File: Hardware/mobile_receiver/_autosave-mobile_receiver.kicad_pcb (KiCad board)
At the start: 4 copper layers, 82.5 x 142 mm, 33 parts, among them J1 Conn_02x07_Top_Bottom, SW1 SW_SPST, SW2 SW_Push, SW3 SW_Push, SW4 SW_Push, SW5 SW_Push, SW6 SW_Push, SW7 SW_Push, U2 kb2040

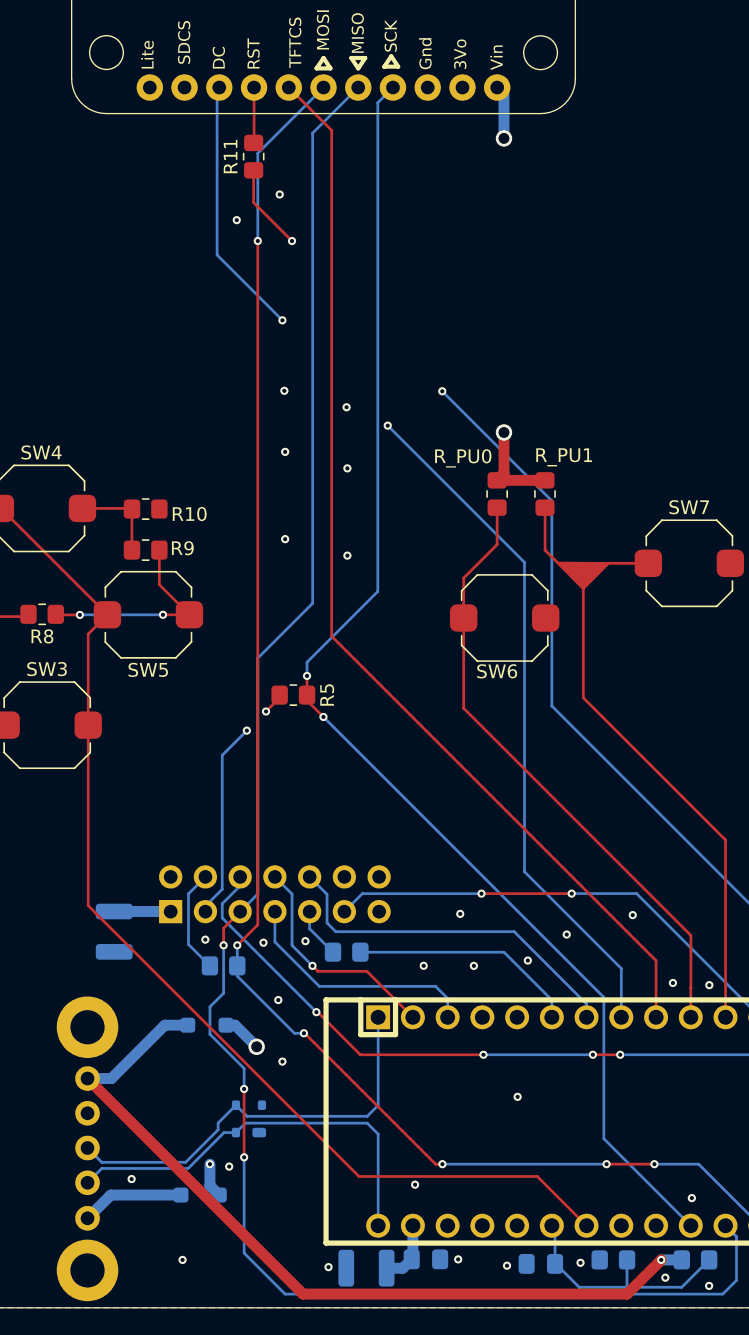
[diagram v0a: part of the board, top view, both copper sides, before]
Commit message: Refined Stitching Vias
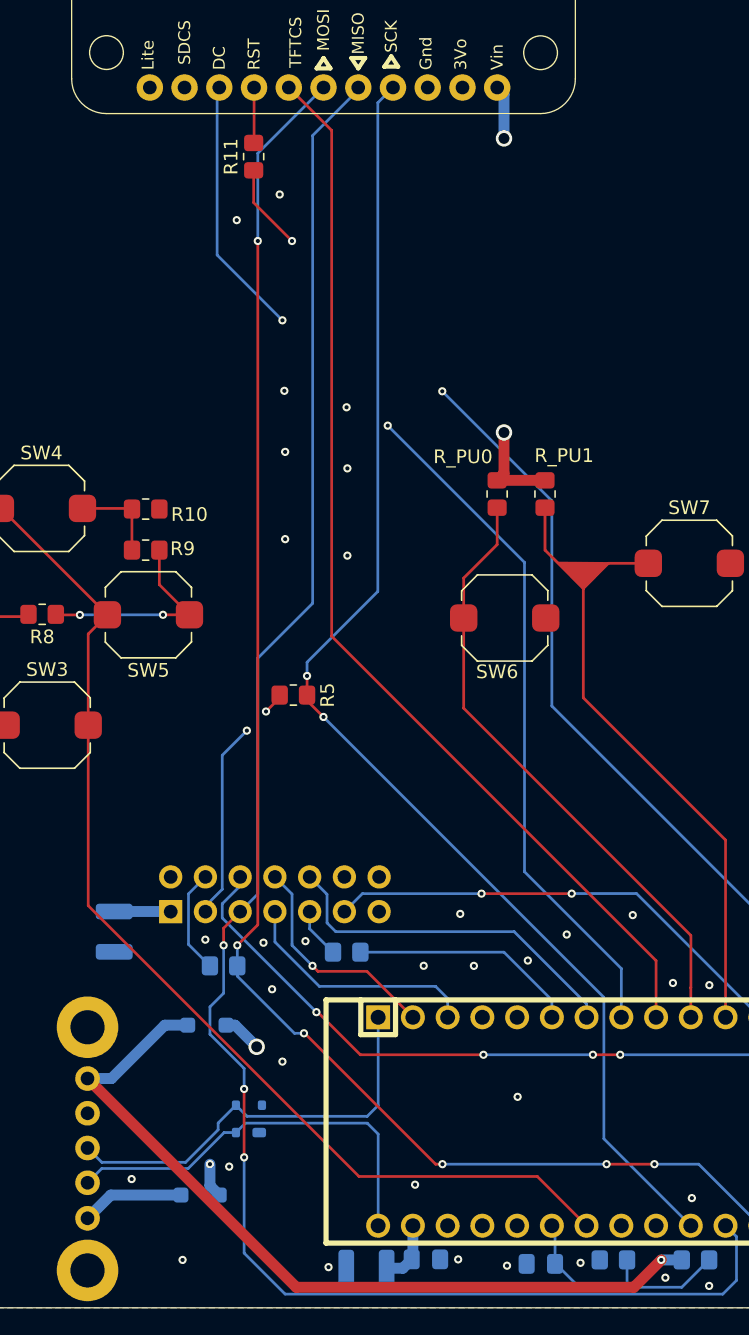
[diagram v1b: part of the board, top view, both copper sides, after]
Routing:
- net +3.3V: track 147.4 -> 148.1 mm
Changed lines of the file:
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@@
 			)
 		)
-		(fp_text user "RT"
-			(at -16.985573 15.83562 90)
-			(unlocked yes)
-			(layer "B.SilkS")
-			(effects
-				(font
-					(size 0.87376 0.87376)
-					(thickness 0.14224)
-				)
-				(justify left mirror)
-			)
-		)
-		(fp_text user "CK"
-			(at -6.825573 15.83562 90)
-			(unlocked yes)
-			(layer "B.SilkS")
-			(effects
-				(font
-					(size 0.87376 0.87376)
-					(thickness 0.14224)
-				)
-				(justify left mirror)
-			)
-		)
-		(fp_text user "SI"
-			(at -11.905573 15.83562 90)
-			(unlocked yes)
-			(layer "B.SilkS")
-			(effects
-				(font
-					(size 0.87376 0.87376)
-					(thickness 0.14224)
-				)
-				(justify left mirror)
-			)
-		)
-		(fp_text user "CC"
-			(at -22.065573 15.83562 90)
-			(unlocked yes)
-			(layer "B.SilkS")
-			(effects
-				(font
-					(size 0.87376 0.87376)
-					(thickness 0.14224)
-				)
-				(justify left mirror)
-			)
-		)
-		(fp_text user "SO"
-			(at -9.365573 15.83562 90)
-			(unlocked yes)
-			(layer "B.SilkS")
-			(effects
-				(font
-					(size 0.87376 0.87376)
-					(thickness 0.14224)
-				)
-				(justify left mirror)
-			)
-		)
-		(fp_text user "V+"
-			(at 0.794427 15.83562 90)
-			(unlocked yes)
-			(layer "B.SilkS")
-			(effects
-				(font
-					(size 0.87376 0.87376)
-					(thickness 0.14224)
-				)
-				(justify left mirror)
-			)
-		)
-		(fp_text user "BL"
-			(at -24.605573 15.83562 90)
-			(unlocked yes)
-			(layer "B.SilkS")
-			(effects
-				(font
-					(size 0.87376 0.87376)
-					(thickness 0.14224)
-				)
-				(justify left mirror)
-			)
-		)
-		(fp_text user "3V"
-			(at -1.745573 15.83562 90)
-			(unlocked yes)
-			(layer "B.SilkS")
-			(effects
-				(font
-					(size 0.87376 0.87376)
-					(thickness 0.14224)
-				)
-				(justify left mirror)
-			)
-		)
-		(fp_text user "G"
-			(at -4.285573 15.83562 90)
-			(unlocked yes)
-			(layer "B.SilkS")
-			(effects
-				(font
-					(size 0.87376 0.87376)
-					(thickness 0.14224)
-				)
-				(justify left mirror)
-			)
-		)
-		(fp_text user "TC"
-			(at -14.445573 15.83562 90)
-			(unlocked yes)
-			(layer "B.SilkS")
-			(effects
-				(font
-					(size 0.87376 0.87376)
-					(thickness 0.14224)
-				)
-				(justify left mirror)
-			)
-		)
-		(fp_text user "DC"
-			(at -19.525573 15.83562 90)
-			(unlocked yes)
-			(layer "B.SilkS")
-			(effects
-				(font
-					(size 0.87376 0.87376)
-					(thickness 0.14224)
-				)
-				(justify left mirror)
-			)
-		)
 		(pad "1" thru_hole circle
 			(at 0.794427 16.97862 270)
@@
 	)
 	(via
-		(at 204.5 199.5)
+		(at 204.045384 198.709131)
 		(size 0.6)
 		(drill 0.3)
@@
 	)
 	(segment
-		(start 230 221)
-		(end 206.311557 221)
+		(start 205.811557 220.5)
+		(end 190.549921 205.238364)
 		(width 0.8)
 		(layer "F.Cu")
@@
 	)
 	(segment
-		(start 206.311557 221)
-		(end 190.549921 205.238364)
+		(start 230.5 220.5)
+		(end 205.811557 220.5)
 		(width 0.8)
 		(layer "F.Cu")
@@
 	(segment
 		(start 232.5 218.5)
-		(end 230 221)
+		(end 230.5 220.5)
 		(width 0.8)
 		(layer "F.Cu")
@@
 	)
 	(segment
-		(start 203 191.747824)
-		(end 203 174.5)
-		(width 0.2)
-		(layer "B.Cu")
-		(net 14)
-	)
-	(segment
 		(start 237 221)
 		(end 205 221)
@@
 	)
 	(segment
-		(start 207.01 170.49)
-		(end 207.01 136.113047)
+		(start 207.01 136.287009)
+		(end 210.344427 132.952582)
 		(width 0.2)
 		(layer "B.Cu")
@@
 	)
 	(segment
+		(start 207.01 170.49)
+		(end 207.01 136.287009)
+		(width 0.2)
+		(layer "B.Cu")
+		(net 14)
+	)
+	(segment
 		(start 199.5 202)
 		(end 199.5 200)
@@
 	)
 	(segment
-		(start 207.01 136.113047)
-		(end 210.344427 132.77862)
+		(start 202 218)
+		(end 202 211)
 		(width 0.2)
 		(layer "B.Cu")
@@
 	)
 	(segment
-		(start 201.710805 193.037019)
-		(end 203 191.747824)
+		(start 238 220)
+		(end 237 221)
 		(width 0.2)
 		(layer "B.Cu")
@@
 	)
 	(segment
-		(start 202 218)
-		(end 202 211)
+		(start 202 206)
+		(end 202 204.5)
 		(width 0.2)
 		(layer "B.Cu")
@@
 	)
 	(segment
-		(start 238 220)
-		(end 237 221)
+		(start 201.710805 193.037019)
+		(end 203 191.747824)
 		(width 0.2)
 		(layer "B.Cu")
@@
 	)
 	(segment
-		(start 202 206)
-		(end 202 204.5)
+		(start 210.344427 132.952582)
+		(end 210.344427 132.77862)
 		(width 0.2)
 		(layer "B.Cu")
@@
 	)
 	(segment
-		(start 199.5 200)
-		(end 200.5 199)
+		(start 203 174.5)
+		(end 207.01 170.49)
 		(width 0.2)
 		(layer "B.Cu")
@@
 	)
 	(segment
-		(start 237.2 216)
-		(end 238 216.8)
+		(start 203 191.747824)
+		(end 203 174.5)
 		(width 0.2)
 		(layer "B.Cu")
@@
 	)
 	(segment
-		(start 203 174.5)
-		(end 207.01 170.49)
+		(start 199.5 200)
+		(end 200.5 199)
+		(width 0.2)
+		(layer "B.Cu")
+		(net 14)
+	)
+	(segment
+		(start 237.2 216)
+		(end 238 216.8)
 		(width 0.2)
 		(layer "B.Cu")
@@
 	)
 	(segment
-		(start 192.5 193.025)
-		(end 196.618786 193.025)
+		(start 221 133.274193)
+		(end 220.504427 132.77862)
 		(width 0.8)
 		(layer "B.Cu")
@@
 	)
 	(segment
-		(start 221 136.5)
-		(end 221 133.274193)
+		(start 192.5 193.025)
+		(end 196.618786 193.025)
 		(width 0.8)
 		(layer "B.Cu")
@@
 		(width 0.8)
 		(layer "B.Cu")
+		(net 34)
+	)
+	(segment
+		(start 221 136.5)
+		(end 221 133.274193)
+		(width 0.8)
+		(layer "B.Cu")
